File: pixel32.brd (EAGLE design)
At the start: 50 x 40 mm, 124 parts, among them CON1 B7B-PH-K-S-SIDE, CON10 PINHEAD_1X01-2.54, CON11 PINHEAD_1X01-2.54, CON12 PINHEAD_1X02-2.54, CON13 PINHEAD_1X07-2, CON14 PINHEAD_1X07-2, CON2 B7B-PH-K-S-SIDE, CON3 PINHEAD_1X02-2.54, CON4 PINHEAD_1X01-2.54, CON5 PINHEAD_1X01-2.54, CON6 PINHEAD_1X01-2.54, CON7 PINHEAD_1X01-2.54, CON8 PINHEAD_1X01-2.54, CON9 PINHEAD_1X01-2.54, IC1 STM32F030K6TX-LQFP32(7X7), IC101 IRS44273L, IC201 IRS44273L, IC3 ST3485SOIC8, IC301 IRS44273L, IC6 MC74VHC1GT125, IC7 MC74VHC1GT125, IC8 LM317, Q101 N-FET-SOT23, Q201 N-FET-SOT23, Q301 N-FET-SOT23, Y1 16MHz

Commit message: Minor changes
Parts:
- moved U$1 1.10 mm to (4.03, 9.20)
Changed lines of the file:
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@@
 <grid distance="0.025" unitdist="mm" unit="mm" style="lines" multiple="2" display="yes" altdistance="0.5" altunitdist="mm" altunit="mm"/>
 <layers>
-<layer number="1" name="Top" color="4" fill="1" visible="yes" active="yes"/>
+<layer number="1" name="Top" color="4" fill="1" visible="no" active="yes"/>
 <layer number="2" name="Route2" color="1" fill="3" visible="no" active="no"/>
 <layer number="3" name="Route3" color="4" fill="3" visible="no" active="no"/>
@@
 <layer number="14" name="Route14" color="1" fill="6" visible="no" active="no"/>
 <layer number="15" name="Route15" color="4" fill="6" visible="no" active="no"/>
-<layer number="16" name="Bottom" color="1" fill="1" visible="no" active="yes"/>
+<layer number="16" name="Bottom" color="1" fill="1" visible="yes" active="yes"/>
 <layer number="17" name="Pads" color="2" fill="1" visible="yes" active="yes"/>
 <layer number="18" name="Vias" color="2" fill="1" visible="yes" active="yes"/>
 <layer number="19" name="Unrouted" color="6" fill="1" visible="yes" active="yes"/>
 <layer number="20" name="Dimension" color="15" fill="1" visible="yes" active="yes"/>
-<layer number="21" name="tPlace" color="7" fill="1" visible="yes" active="yes"/>
-<layer number="22" name="bPlace" color="7" fill="1" visible="no" active="yes"/>
-<layer number="23" name="tOrigins" color="15" fill="1" visible="yes" active="yes"/>
-<layer number="24" name="bOrigins" color="15" fill="1" visible="no" active="yes"/>
-<layer number="25" name="tNames" color="7" fill="1" visible="yes" active="yes"/>
-<layer number="26" name="bNames" color="7" fill="1" visible="no" active="yes"/>
+<layer number="21" name="tPlace" color="7" fill="1" visible="no" active="yes"/>
+<layer number="22" name="bPlace" color="7" fill="1" visible="yes" active="yes"/>
+<layer number="23" name="tOrigins" color="15" fill="1" visible="no" active="yes"/>
+<layer number="24" name="bOrigins" color="15" fill="1" visible="yes" active="yes"/>
+<layer number="25" name="tNames" color="7" fill="1" visible="no" active="yes"/>
+<layer number="26" name="bNames" color="7" fill="1" visible="yes" active="yes"/>
 <layer number="27" name="tValues" color="7" fill="1" visible="no" active="yes"/>
 <layer number="28" name="bValues" color="7" fill="1" visible="no" active="yes"/>
@@
 <layer number="49" name="Reference" color="7" fill="1" visible="no" active="yes"/>
 <layer number="50" name="dxf" color="7" fill="1" visible="no" active="no"/>
-<layer number="51" name="tDocu" color="7" fill="1" visible="yes" active="yes"/>
-<layer number="52" name="bDocu" color="7" fill="1" visible="no" active="yes"/>
+<layer number="51" name="tDocu" color="7" fill="1" visible="no" active="yes"/>
+<layer number="52" name="bDocu" color="7" fill="1" visible="yes" active="yes"/>
 <layer number="53" name="tGND_GNDA" color="7" fill="9" visible="no" active="no"/>
 <layer number="54" name="bGND_GNDA" color="1" fill="9" visible="no" active="no"/>
@@
 <attribute name="FARNELL#" value="1749366" x="-17.1" y="2.1" size="1.778" layer="27" display="off"/>
 </element>
-<element name="U$1" library="logo" package="RTU" value="" x="5.125" y="9.25" rot="MR0"/>
+<element name="U$1" library="logo" package="RTU" value="" x="4.025" y="9.2" rot="MR0"/>
 <element name="CON13" library="pinhead" package="1X07-PTH-2" value="PINHEAD_1X07-2" x="-18.44" y="12" rot="R270"/>
 <element name="CON14" library="pinhead" package="1X07-PTH-2" value="PINHEAD_1X07-2" x="18.44" y="12" rot="R90"/>

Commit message: Minor fixes
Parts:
- added DRILEGEND: (no value), drilegend:DRILEGEND
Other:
- board text added: "01-16"
- board text added: "01-20"
- board text added: "LAYER-STACK"

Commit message: minor updates
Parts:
- added SJ5: (no value), eth_conv_master_lib:RES_0
- moved U$3 6.50 mm to (15.0, 5.50), flipped to the top, turned to 180 degrees
- moved R9 4.75 mm to (9.45, 8.03), turned to 180 degrees
- moved U$6 4.51 mm to (15.0, 6.50), flipped to the top, turned to 180 degrees
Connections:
- net RX: now also SJ5.2
- net TX: now also SJ5.1
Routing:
- net TX: track 3.08 -> 7.98 mm, vias 0 -> 1
- net GNDD: track 56.9 -> 53.2 mm
- net VDD_3V3: track 63.9 -> 63.5 mm, vias 9 -> 10
- net RX: track 5.86 -> 6.21 mm, vias 0 -> 1
- net GND: vias 111 -> 121

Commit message: Minor fixes
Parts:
- added U$10, U$7, U$8, U$9: CONNECTION, usb2can_master_lib:CONNECTION
- moved U$3 0.25 mm to (15.2, 5.65)
- moved U$6 0.15 mm to (15.0, 6.35)
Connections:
- net GND: now also U$10.P$2, U$7.P$2, U$8.P$2, U$9.P$2
- net GNDD: now also U$10.P$1, U$7.P$1, U$8.P$1, U$9.P$1
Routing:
- net GND: vias 121 -> 123
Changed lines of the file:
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@@
 <setting verticaltext="up"/>
 </settings>
-<grid distance="0.05" unitdist="mm" unit="mm" style="lines" multiple="2" display="yes" altdistance="0.5" altunitdist="mm" altunit="mm"/>
+<grid distance="0.025" unitdist="mm" unit="mm" style="lines" multiple="2" display="yes" altdistance="0.5" altunitdist="mm" altunit="mm"/>
 <layers>
 <layer number="1" name="Top" color="4" fill="1" visible="yes" active="yes"/>
@@
 <layer number="27" name="tValues" color="7" fill="1" visible="no" active="yes"/>
 <layer number="28" name="bValues" color="7" fill="1" visible="no" active="yes"/>
-<layer number="29" name="tStop" color="7" fill="6" visible="no" active="yes"/>
+<layer number="29" name="tStop" color="7" fill="6" visible="yes" active="yes"/>
 <layer number="30" name="bStop" color="7" fill="3" visible="no" active="yes"/>
 <layer number="31" name="tCream" color="7" fill="5" visible="no" active="yes"/>
@@
 <attribute name="TME#" value="RC0603FR-0710K" x="2.7" y="4.075" size="1.778" layer="27" display="off"/>
 </element>
-<element name="U$6" library="usb2can_master_lib" package="CONNECTION" value="CONNECTION" x="14.975" y="6.5" rot="R180">
-<attribute name="BOM" value="EXCLUDE" x="17" y="3.15" size="1.778" layer="27" rot="R180" display="off"/>
+<element name="U$6" library="usb2can_master_lib" package="CONNECTION" value="CONNECTION" x="14.975" y="6.35" rot="R180">
+<attribute name="BOM" value="EXCLUDE" x="17" y="3" size="1.778" layer="27" rot="R180" display="off"/>
 </element>
 <element name="SJ1" library="eth_conv_master_lib" package="RES_0" value="" x="-17.45" y="-1.025" smashed="yes">
@@
 <attribute name="BOM" value="EXCLUDE" x="-13.025" y="-2.125" size="1.778" layer="28" rot="MR270" display="off"/>
 </element>
-<element name="U$3" library="usb2can_master_lib" package="CONNECTION" value="CONNECTION" x="14.975" y="5.5" rot="R180">
-<attribute name="BOM" value="EXCLUDE" x="14.975" y="5.5" size="1.778" layer="27" rot="R180" display="off"/>
+<element name="U$3" library="usb2can_master_lib" package="CONNECTION" value="CONNECTION" x="15.175" y="5.65" rot="R180">
+<attribute name="BOM" value="EXCLUDE" x="15.175" y="5.65" size="1.778" layer="27" rot="R180" display="off"/>
 </element>
 <element name="PAD3" library="wirepad" package="PAD-2.5-1.8" value="WIREPADSMD2.5-1.8" x="12.8" y="18.3">
@@
 <element name="SJ5" library="eth_conv_master_lib" package="RES_0" value="" x="-6.4" y="4.35" rot="MR180">
 <attribute name="BOM" value="EXCLUDE" x="-6.4" y="4.35" size="1.778" layer="28" rot="MR180" display="off"/>
+</element>
+<element name="U$7" library="usb2can_master_lib" package="CONNECTION" value="CONNECTION" x="16.25" y="5.55" rot="R270">
+<attribute name="BOM" value="EXCLUDE" x="16.25" y="5.55" size="1.778" layer="27" rot="R270" display="off"/>
+</element>
+<element name="U$8" library="usb2can_master_lib" package="CONNECTION" value="CONNECTION" x="15.25" y="5.55" rot="R270">
+<attribute name="BOM" value="EXCLUDE" x="15.25" y="5.55" size="1.778" layer="27" rot="R270" display="off"/>
+</element>
+<element name="U$9" library="usb2can_master_lib" package="CONNECTION" value="CONNECTION" x="17.25" y="5.55" rot="R270">
+<attribute name="BOM" value="EXCLUDE" x="17.25" y="5.55" size="1.778" layer="27" rot="R270" display="off"/>
+</element>
+<element name="U$10" library="usb2can_master_lib" package="CONNECTION" value="CONNECTION" x="17.6" y="5.55" rot="R270">
+<attribute name="BOM" value="EXCLUDE" x="17.6" y="5.55" size="1.778" layer="27" rot="R270" display="off"/>
 </element>
 </elements>
@@
 <via x="0.575" y="9.35" extent="1-16" drill="0.3"/>
 <via x="-3.025" y="9.875" extent="1-16" drill="0.3"/>
-<via x="9.55" y="5.775" extent="1-16" drill="0.3"/>
-<via x="10.5" y="5.775" extent="1-16" drill="0.3"/>
-<via x="9.1" y="6.25" extent="1-16" drill="0.3"/>
-<via x="10" y="6.25" extent="1-16" drill="0.3"/>
+<via x="10.5" y="6.125" extent="1-16" drill="0.3"/>
+<via x="11.5" y="5.225" extent="1-16" drill="0.3"/>
+<via x="8.95" y="6.55" extent="1-16" drill="0.3"/>
+<via x="11.7" y="6.1" extent="1-16" drill="0.3"/>
 <via x="-2.275" y="1.85" extent="1-16" drill="0.3"/>
 <via x="-2.275" y="0.7" extent="1-16" drill="0.3"/>
@@
 <via x="-0.6" y="12.975" extent="1-16" drill="0.3"/>
 <via x="1.025" y="10.75" extent="1-16" drill="0.3"/>
-<via x="14.05" y="5.125" extent="1-16" drill="0.3"/>
-<via x="14.05" y="6.225" extent="1-16" drill="0.3"/>
-<via x="14.05" y="7.325" extent="1-16" drill="0.3"/>
-<via x="14.05" y="8.425" extent="1-16" drill="0.3"/>
-<via x="13.5" y="7.875" extent="1-16" drill="0.3"/>
-<via x="13.5" y="6.775" extent="1-16" drill="0.3"/>
-<via x="13.5" y="5.675" extent="1-16" drill="0.3"/>
-<via x="12.95" y="6.225" extent="1-16" drill="0.3"/>
-<via x="12.95" y="7.325" extent="1-16" drill="0.3"/>
-<via x="12.95" y="8.425" extent="1-16" drill="0.3"/>
-<via x="17.5" y="4.475" extent="1-16" drill="0.3"/>
-<via x="16.7" y="4.475" extent="1-16" drill="0.3"/>
-<via x="15.85" y="4.475" extent="1-16" drill="0.3"/>
-<via x="14.85" y="4.475" extent="1-16" drill="0.3"/>
+<via x="14.45" y="5.375" extent="1-16" drill="0.3"/>
+<via x="14.5" y="7.125" extent="1-16" drill="0.3"/>
+<via x="14.3" y="8.175" extent="1-16" drill="0.3"/>
+<via x="13.95" y="8.925" extent="1-16" drill="0.3"/>
+<via x="13.5" y="7.625" extent="1-16" drill="0.3"/>
+<via x="12.35" y="7.725" extent="1-16" drill="0.3"/>
+<via x="13.35" y="6.575" extent="1-16" drill="0.3"/>
+<via x="12.75" y="8.775" extent="1-16" drill="0.3"/>
+<via x="11.3" y="8.075" extent="1-16" drill="0.3"/>
+<via x="17.5" y="4.625" extent="1-16" drill="0.3"/>
+<via x="16.7" y="4.625" extent="1-16" drill="0.3"/>
+<via x="15.85" y="4.625" extent="1-16" drill="0.3"/>
+<via x="15.1" y="4.625" extent="1-16" drill="0.3"/>
 <via x="-4.325" y="-8.6" extent="1-16" drill="0.3"/>
+<contactref element="U$9" pad="P$2"/>
+<contactref element="U$7" pad="P$2"/>
+<contactref element="U$8" pad="P$2"/>
+<contactref element="U$10" pad="P$2"/>
+<via x="9.35" y="5.525" extent="1-16" drill="0.3"/>
+<via x="6.6" y="7.175" extent="1-16" drill="0.3"/>
+<via x="13.6" y="4.275" extent="1-16" drill="0.3"/>
 </signal>
 <signal name="N$49">
@@
 <contactref element="IC1" pad="20"/>
 <wire x1="2.65" y1="10.9" x2="5.05" y2="10.9" width="0.3" layer="1"/>
-<wire x1="15.375" y1="2.825" x2="15.1" y2="2.825" width="0.3" layer="1"/>
-<via x="11.5" y="5.15" extent="1-16" drill="0.3"/>
-<wire x1="10.375" y1="7" x2="11.525" y2="5.85" width="0.3" layer="1"/>
-<wire x1="15.1" y1="2.825" x2="13.775" y2="4.15" width="0.3" layer="1"/>
-<wire x1="10.375" y1="7" x2="9.5" y2="7" width="0.3" layer="1"/>
+<wire x1="15.375" y1="2.825" x2="14.925" y2="2.825" width="0.3" layer="1"/>
+<via x="13.55" y="5.25" extent="1-16" drill="0.3"/>
 <wire x1="9.5" y1="7" x2="8.725" y2="7.775" width="0.3" layer="1"/>
 <wire x1="8.725" y1="7.775" x2="8.725" y2="8.025" width="0.3" layer="1"/>
-<wire x1="5.05" y1="10.9" x2="7.65" y2="8.3" width="0.3" layer="1"/>
-<wire x1="7.65" y1="8.3" x2="8.725" y2="8.3" width="0.3" layer="1"/>
-<wire x1="8.725" y1="8.3" x2="8.725" y2="8.025" width="0.3" layer="1"/>
-<wire x1="13.775" y1="4.15" x2="12.5" y2="4.15" width="0.3" layer="1"/>
-<wire x1="12.5" y1="4.15" x2="11.5" y2="5.15" width="0.3" layer="1"/>
-<wire x1="11.525" y1="5.85" x2="11.525" y2="5.175" width="0.3" layer="1"/>
-<wire x1="11.525" y1="5.175" x2="11.5" y2="5.15" width="0.3" layer="1"/>
+<wire x1="5.05" y1="10.9" x2="7.925" y2="8.025" width="0.3" layer="1"/>
 <wire x1="12.55" y1="4.65" x2="12.25" y2="4.65" width="0.3" layer="16"/>
-<wire x1="11.95" y1="5.15" x2="11.5" y2="5.15" width="0.3" layer="16"/>
-<wire x1="11.95" y1="5.15" x2="12.45" y2="4.65" width="0.3" layer="16"/>
 <wire x1="12.45" y1="4.65" x2="12.55" y2="4.65" width="0.3" layer="16"/>
+<wire x1="9.5" y1="7" x2="11.8" y2="7" width="0.3" layer="1"/>
+<wire x1="12.55" y1="4.65" x2="12.95" y2="4.65" width="0.3" layer="16"/>
+<wire x1="12.95" y1="4.65" x2="13.55" y2="5.25" width="0.3" layer="16"/>
+<wire x1="11.8" y1="7" x2="13.55" y2="5.25" width="0.3" layer="1"/>
+<wire x1="7.925" y1="8.025" x2="8.725" y2="8.025" width="0.3" layer="1"/>
+<wire x1="13.55" y1="5.25" x2="14.925" y2="3.875" width="0.3" layer="1"/>
+<wire x1="14.925" y1="2.825" x2="14.925" y2="3.875" width="0.3" layer="1"/>
 </signal>
 <signal name="LED2_PWM">
@@
 <contactref element="IC301" pad="4"/>
 <contactref element="IC301" pad="3"/>
-<wire x1="4.5" y1="0.925" x2="4.975" y2="0.925" width="0.3" layer="1"/>
-<wire x1="4.975" y1="0.925" x2="4.975" y2="0.225" width="0.3" layer="1"/>
-<wire x1="4.975" y1="0.225" x2="5.6" y2="-0.4" width="0.3" layer="1"/>
+<wire x1="4.95" y1="0.25" x2="5.6" y2="-0.4" width="0.3" layer="1"/>
 <wire x1="1.9" y1="0.925" x2="3.15" y2="0.925" width="0.3" layer="1"/>
 <wire x1="3.15" y1="0.925" x2="4.5" y2="0.925" width="0.3" layer="1"/>
 <wire x1="3.2" y1="1.15" x2="3.2" y2="0.975" width="0.3" layer="1"/>
 <wire x1="3.2" y1="0.975" x2="3.15" y2="0.925" width="0.3" layer="1"/>
+<wire x1="4.95" y1="0.25" x2="4.95" y2="0.925" width="0.3" layer="1"/>
+<wire x1="4.95" y1="0.925" x2="4.5" y2="0.925" width="0.3" layer="1"/>
 </signal>
 <signal name="N$10">
@@
 <wire x1="-11.975" y1="18.375" x2="-5.4" y2="18.375" width="0.2" layer="1"/>
 <wire x1="-5.4" y1="18.375" x2="-5.4" y2="18.725" width="0.2" layer="1"/>
+<contactref element="U$9" pad="P$1"/>
+<contactref element="U$8" pad="P$1"/>
+<contactref element="U$7" pad="P$1"/>
+<contactref element="U$10" pad="P$1"/>
 </signal>
 <signal name="N$13">

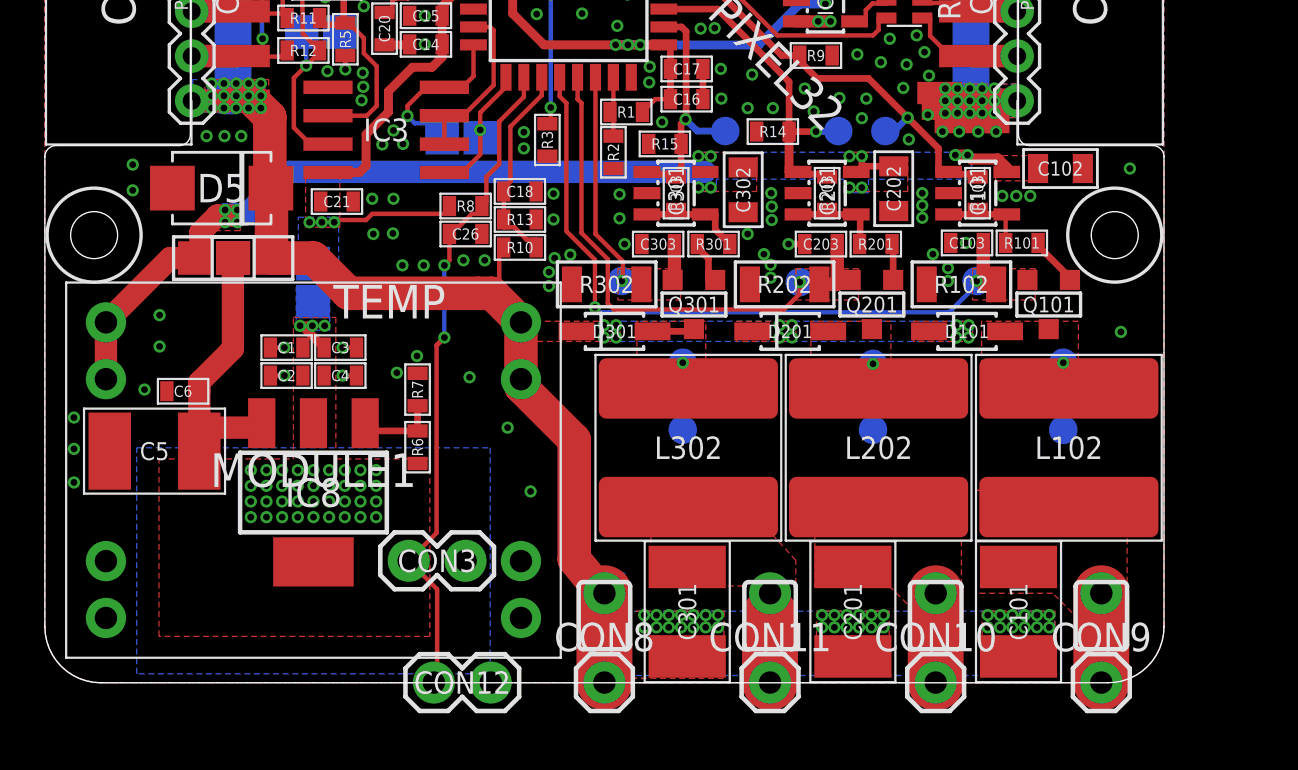
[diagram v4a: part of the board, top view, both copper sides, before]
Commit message: Added spare power connector just in case. New 3d view.
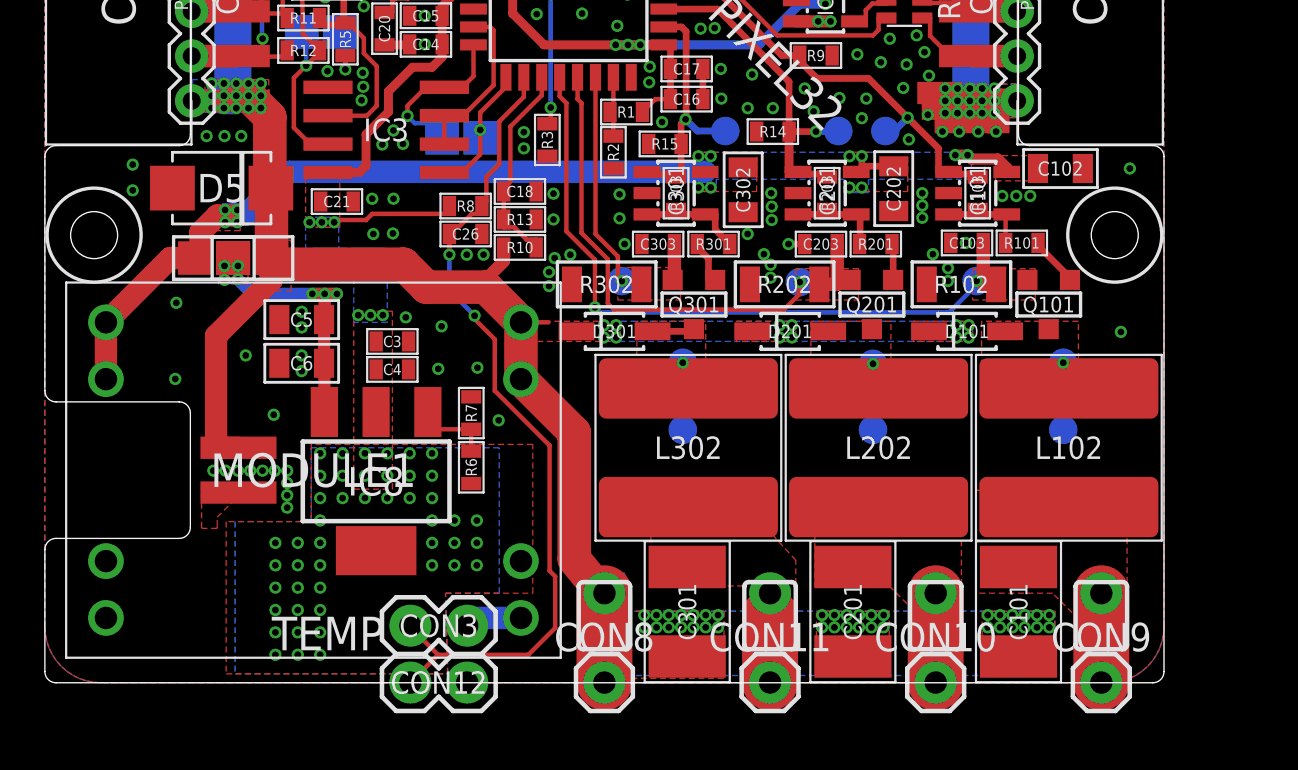
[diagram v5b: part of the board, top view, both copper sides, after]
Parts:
- removed C1, C2: 4.7 uF, rc:C0603
- added CON15: (no value), led_matrix_master_lib:B2B-PH-K-S_SIDE_MOUNT
- C5: value 10 uF -> 100 nF; device rc:C1812 -> rc:C0805
- C6: device rc:C0603 -> rc:C0805
- moved C5 8.82 mm to (-13.5, -3.77)
- moved C6 5.45 mm to (-13.5, -5.72)
- moved CON3 2.90 mm to (-7.40, -17.4)
- moved IC8 2.84 mm to (-10.2, -11.0)
- moved R7 2.62 mm to (-5.95, -7.95)
- moved R6 2.56 mm to (-5.95, -10.4)
- moved C3 2.34 mm to (-9.47, -4.75)
- moved C4 2.34 mm to (-9.47, -6.00)
- moved SJ4 1.82 mm to (-11.4, -1.30), turned to 180 degrees
- moved CON12 1.05 mm to (-7.40, -20.0)
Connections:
- net GND: now also C5.1, CON15.1; no longer C1.1, C2.1, C5.P$1
- net N$2: no longer C1.2, C2.2
- net N$5: now also C5.2; no longer C5.P$2
- net VDD_24V: now also CON15.2
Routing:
- net VDD_24V: track 91.6 -> 103.2 mm
- net TEMP: track 30.7 -> 37.8 mm
- net N$2: track 2.01 -> 0.00 mm, vias 39 -> 49
- net N$5: track 12.2 -> 11.1 mm, vias 0 -> 7
- net GND: track 9.42 -> 9.46 mm, vias 123 -> 129
- added copper zone on layer 1, net N$5
- added copper zone on layer 16, net N$5
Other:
- outline, holes or cut-outs redrawn
